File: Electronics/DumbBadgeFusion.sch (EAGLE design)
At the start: 148 parts, among them IC1 74245MTC, IC2 74245MTC, IC3 74245MTC, SW1 SPST_TACT-KMR2, T1 MMUN2133LT1G, U1 ATSAMD21J18A-AUT, U2 TPS61090RSAR, U3 MCP73871, U4 FAN5333BSX, U5 TDP3E001DRLR-SOT-23-5SOT-23-5, U6 MAX3232, X4 NX3215SA-32.768K-STD-MUA-8

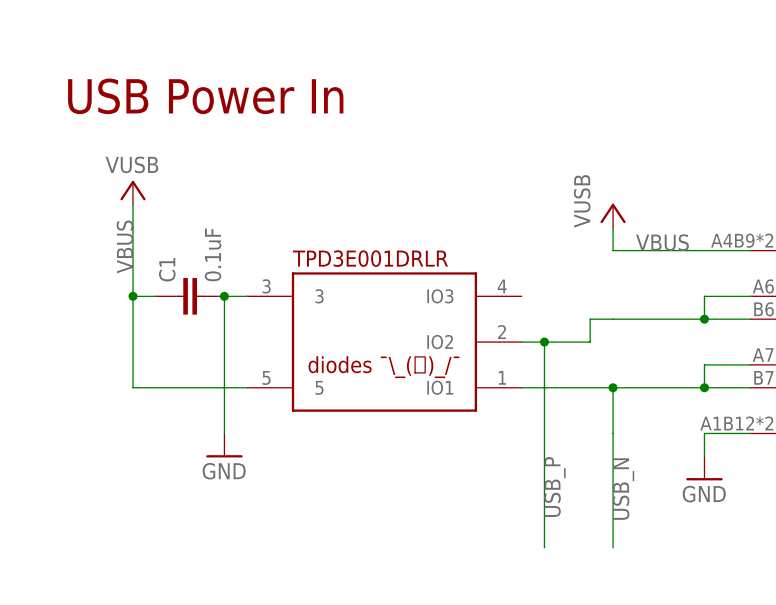
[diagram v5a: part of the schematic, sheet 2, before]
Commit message: Fixed footprint for ESD, D1
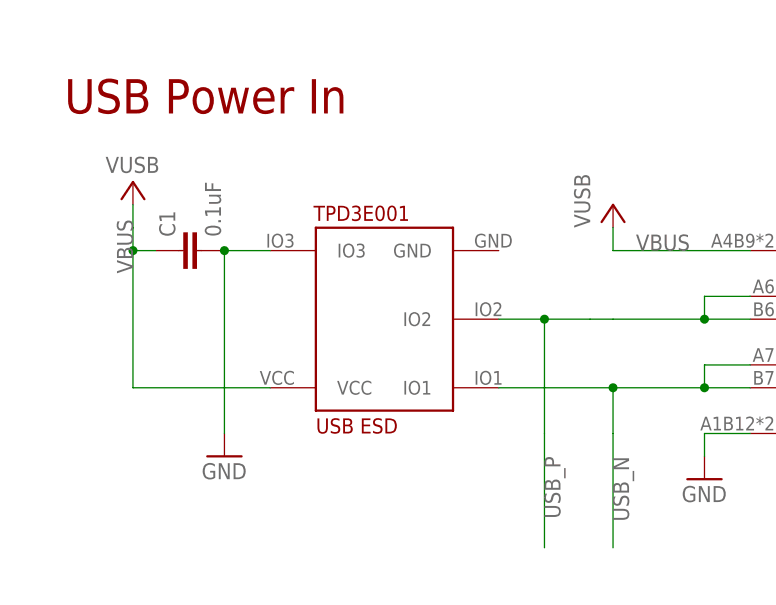
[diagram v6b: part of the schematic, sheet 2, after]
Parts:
- D1: device microbuilder:DIODESMA -> diode:DIODE-SOD323-W
- U5: value TDP3E001DRLR-SOT-23-5SOT-23-5 -> TPD3E001SOT5; device USBC:TDP3E001DRLR-SOT-23-5SOT-23-5 -> FPC:TPD3E001SOT5
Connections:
- net GND: now also U5.IO3; no longer U5.3
- net VBUS: now also U5.VCC; no longer U5.5
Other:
- note removed: "TPD3E001DRLR"
- moved on the sheet: C1
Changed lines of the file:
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@@
 <part name="R3" library="SparkFun-Resistors" library_urn="urn:adsk.eagle:library:532" deviceset="1KOHM" device="-0603-1/10W-1%" package3d_urn="urn:adsk.eagle:package:39650/1" value="5.1k"/>
 <part name="U$6" library="microbuilder" deviceset="GND" device=""/>
-<part name="U5" library="USBC" deviceset="TDP3E001DRLR-SOT-23-5" device="SOT-23-5"/>
+<part name="U5" library="FPC" deviceset="TPD3E001SOT5" device=""/>
 <part name="P+1" library="supply1" library_urn="urn:adsk.eagle:library:371" deviceset="VCC" device="" value="VUSB"/>
 <part name="P+2" library="supply1" library_urn="urn:adsk.eagle:library:371" deviceset="VCC" device="" value="VUSB"/>
@@
 <part name="U$22" library="microbuilder" deviceset="GND" device=""/>
 <part name="U$26" library="microbuilder" deviceset="GND" device=""/>
-<part name="D1" library="microbuilder" deviceset="DIODE" device="SMA" value="MM3Z24VT1G"/>
+<part name="D1" library="diode" library_urn="urn:adsk.eagle:library:210" deviceset="DIODE-" device="SOD323-W" package3d_urn="urn:adsk.eagle:package:43418/1" value="MM3Z24VT1G"/>
 <part name="U$29" library="microbuilder" deviceset="GND" device=""/>
 <part name="C8" library="SparkFun-Capacitors" library_urn="urn:adsk.eagle:library:510" deviceset="1.0UF" device="-0805-25V-10%" package3d_urn="urn:adsk.eagle:package:37429/1" value="10uF"/>
@@
 <description>Power System I</description>
 <plain>
-<text x="33.02" y="229.362" size="1.778" layer="94">TPD3E001DRLR</text>
 <text x="89.154" y="234.696" size="1.778" layer="94">Type-C-31-M-12</text>
 <text x="7.62" y="246.38" size="3.81" layer="94">USB Power In</text>
@@
 <attribute name="VALUE" x="140.716" y="218.44" size="1.27" layer="96"/>
 </instance>
-<instance part="U5" gate="G$1" x="40.64" y="220.98" smashed="yes" rot="R180"/>
+<instance part="U5" gate="G$1" x="43.18" y="223.52" smashed="yes"/>
 <instance part="P+1" gate="VCC" x="68.58" y="236.22" smashed="yes">
 <attribute name="VALUE" x="66.04" y="233.68" size="1.778" layer="96" rot="R90"/>
@@
 <attribute name="VALUE" x="12.192" y="239.776" size="1.778" layer="96"/>
 </instance>
-<instance part="C1" gate="G$1" x="22.86" y="226.06" smashed="yes" rot="R90">
-<attribute name="NAME" x="19.939" y="227.584" size="1.778" layer="95" font="vector" rot="R90"/>
-<attribute name="VALUE" x="25.019" y="227.584" size="1.778" layer="96" font="vector" rot="R90"/>
+<instance part="C1" gate="G$1" x="22.86" y="231.14" smashed="yes" rot="R90">
+<attribute name="NAME" x="19.939" y="232.664" size="1.778" layer="95" font="vector" rot="R90"/>
+<attribute name="VALUE" x="25.019" y="232.664" size="1.778" layer="96" font="vector" rot="R90"/>
 </instance>
 <instance part="GND1" gate="1" x="25.4" y="208.28" smashed="yes">
@@
 </segment>
 <segment>
-<pinref part="U5" gate="G$1" pin="3"/>
 <pinref part="C1" gate="G$1" pin="2"/>
-<wire x1="27.94" y1="226.06" x2="25.4" y2="226.06" width="0.1524" layer="91"/>
-<wire x1="25.4" y1="226.06" x2="25.4" y2="210.82" width="0.1524" layer="91"/>
-<junction x="25.4" y="226.06"/>
+<wire x1="25.4" y1="231.14" x2="25.4" y2="210.82" width="0.1524" layer="91"/>
 <pinref part="GND1" gate="1" pin="GND"/>
+<pinref part="U5" gate="G$1" pin="IO3"/>
+<wire x1="25.4" y1="231.14" x2="30.48" y2="231.14" width="0.1524" layer="91"/>
+<junction x="25.4" y="231.14"/>
 </segment>
 <segment>
@@
 <wire x1="78.74" y1="215.9" x2="68.58" y2="215.9" width="0.1524" layer="91"/>
 <junction x="78.74" y="215.9"/>
+<wire x1="68.58" y1="210.82" x2="68.58" y2="215.9" width="0.1524" layer="91"/>
 <pinref part="U5" gate="G$1" pin="IO1"/>
-<wire x1="68.58" y1="215.9" x2="58.42" y2="215.9" width="0.1524" layer="91"/>
-<wire x1="68.58" y1="210.82" x2="68.58" y2="215.9" width="0.1524" layer="91"/>
+<wire x1="55.88" y1="215.9" x2="68.58" y2="215.9" width="0.1524" layer="91"/>
 <junction x="68.58" y="215.9"/>
 </segment>
@@
 <junction x="78.74" y="223.52"/>
 <wire x1="68.58" y1="223.52" x2="66.04" y2="223.52" width="0.1524" layer="91"/>
-<wire x1="66.04" y1="223.52" x2="66.04" y2="220.98" width="0.1524" layer="91"/>
+<wire x1="66.04" y1="223.52" x2="60.96" y2="223.52" width="0.1524" layer="91"/>
+<wire x1="60.96" y1="210.82" x2="60.96" y2="223.52" width="0.1524" layer="91"/>
 <pinref part="U5" gate="G$1" pin="IO2"/>
-<wire x1="66.04" y1="220.98" x2="60.96" y2="220.98" width="0.1524" layer="91"/>
-<wire x1="60.96" y1="220.98" x2="58.42" y2="220.98" width="0.1524" layer="91"/>
-<wire x1="60.96" y1="210.82" x2="60.96" y2="220.98" width="0.1524" layer="91"/>
-<junction x="60.96" y="220.98"/>
+<wire x1="60.96" y1="223.52" x2="55.88" y2="223.52" width="0.1524" layer="91"/>
+<junction x="60.96" y="223.52"/>
 </segment>
 </net>
@@
 <pinref part="P+2" gate="VCC" pin="VCC"/>
 <wire x1="15.24" y1="236.22" x2="15.24" y2="233.68" width="0.1524" layer="91"/>
-<wire x1="15.24" y1="233.68" x2="15.24" y2="226.06" width="0.1524" layer="91"/>
-<pinref part="U5" gate="G$1" pin="5"/>
-<wire x1="15.24" y1="226.06" x2="15.24" y2="215.9" width="0.1524" layer="91"/>
-<wire x1="15.24" y1="215.9" x2="27.94" y2="215.9" width="0.1524" layer="91"/>
+<wire x1="15.24" y1="233.68" x2="15.24" y2="231.14" width="0.1524" layer="91"/>
+<wire x1="15.24" y1="231.14" x2="15.24" y2="215.9" width="0.1524" layer="91"/>
 <pinref part="C1" gate="G$1" pin="1"/>
-<wire x1="17.78" y1="226.06" x2="15.24" y2="226.06" width="0.1524" layer="91"/>
-<junction x="15.24" y="226.06"/>
+<wire x1="17.78" y1="231.14" x2="15.24" y2="231.14" width="0.1524" layer="91"/>
+<junction x="15.24" y="231.14"/>
 <label x="15.24" y="228.6" size="1.778" layer="95" rot="R90"/>
-</segment>
-<segment>
+<pinref part="U5" gate="G$1" pin="VCC"/>
+<wire x1="30.48" y1="215.9" x2="15.24" y2="215.9" width="0.1524" layer="91"/>
+</segment>
+<segment>

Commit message: stuff changed
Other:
- note added: "Keyboard Matrix"
- moved on the sheet: K-1, K-2, K-5, K_0, K_3, K_4, K_6, K_7, K_8, K_9, K_<, K_>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

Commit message: Getting stuff working
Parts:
- added C12: 1.0uF, SparkFun-Capacitors:1.0UF-0805-25V-10%
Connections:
- new net N$3: C12.1, U1.VDDCORE
- net GND: now also C12.2
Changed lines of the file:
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@@
 <part name="U$30" library="FPC" deviceset="SAMTEC_PI_REVERSE" device=""/>
 <part name="GND20" library="supply1" deviceset="GND" device=""/>
+<part name="C12" library="SparkFun-Capacitors" library_urn="urn:adsk.eagle:library:510" deviceset="1.0UF" device="-0805-25V-10%" package3d_urn="urn:adsk.eagle:package:37429/1" value="1.0uF"/>
+<part name="GND12" library="supply1" deviceset="GND" device=""/>
 </parts>
 <sheets>
@@
 <attribute name="NAME" x="220.98" y="166.624" size="1.778" layer="95" font="vector" align="bottom-center"/>
 <attribute name="VALUE" x="220.98" y="163.576" size="1.778" layer="96" font="vector" align="top-center"/>
+</instance>
+<instance part="C12" gate="G$1" x="10.16" y="73.66" smashed="yes">
+<attribute name="NAME" x="11.684" y="76.581" size="1.778" layer="95" font="vector"/>
+<attribute name="VALUE" x="11.684" y="71.501" size="1.778" layer="96" font="vector"/>
+</instance>
+<instance part="GND12" gate="1" x="10.16" y="31.75" smashed="yes">
+<attribute name="VALUE" x="7.62" y="29.21" size="1.778" layer="96"/>
 </instance>
 </instances>
@@
 <junction x="20.32" y="12.7"/>
 </segment>
+<segment>
+<pinref part="C12" gate="G$1" pin="2"/>
+<wire x1="10.16" y1="71.12" x2="10.16" y2="38.1" width="0.1524" layer="91"/>
+<pinref part="GND12" gate="1" pin="GND"/>
+<wire x1="10.16" y1="38.1" x2="10.16" y2="34.29" width="0.1524" layer="91"/>
+</segment>
 </net>
 <net name="SWCLK" class="0">
@@
 </segment>
 </net>
+<net name="N$3" class="0">
+<segment>
+<pinref part="U1" gate="G$1" pin="VDDCORE"/>
+<pinref part="C12" gate="G$1" pin="1"/>
+<wire x1="30.48" y1="78.74" x2="10.16" y2="78.74" width="0.1524" layer="91"/>
+</segment>
+</net>
